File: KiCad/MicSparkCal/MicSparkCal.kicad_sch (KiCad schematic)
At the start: 36 parts, among them J1 Cortex Debug, J10 TF_S_A, J11 TF_S_B, J12 HV_A, J13 HV_B, J2 ON/OFF, J3 BOOST_IN_P, J4 BOOST_IN_N, J5 BOOST_OUT_P, J6 BOOST_OUT_N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

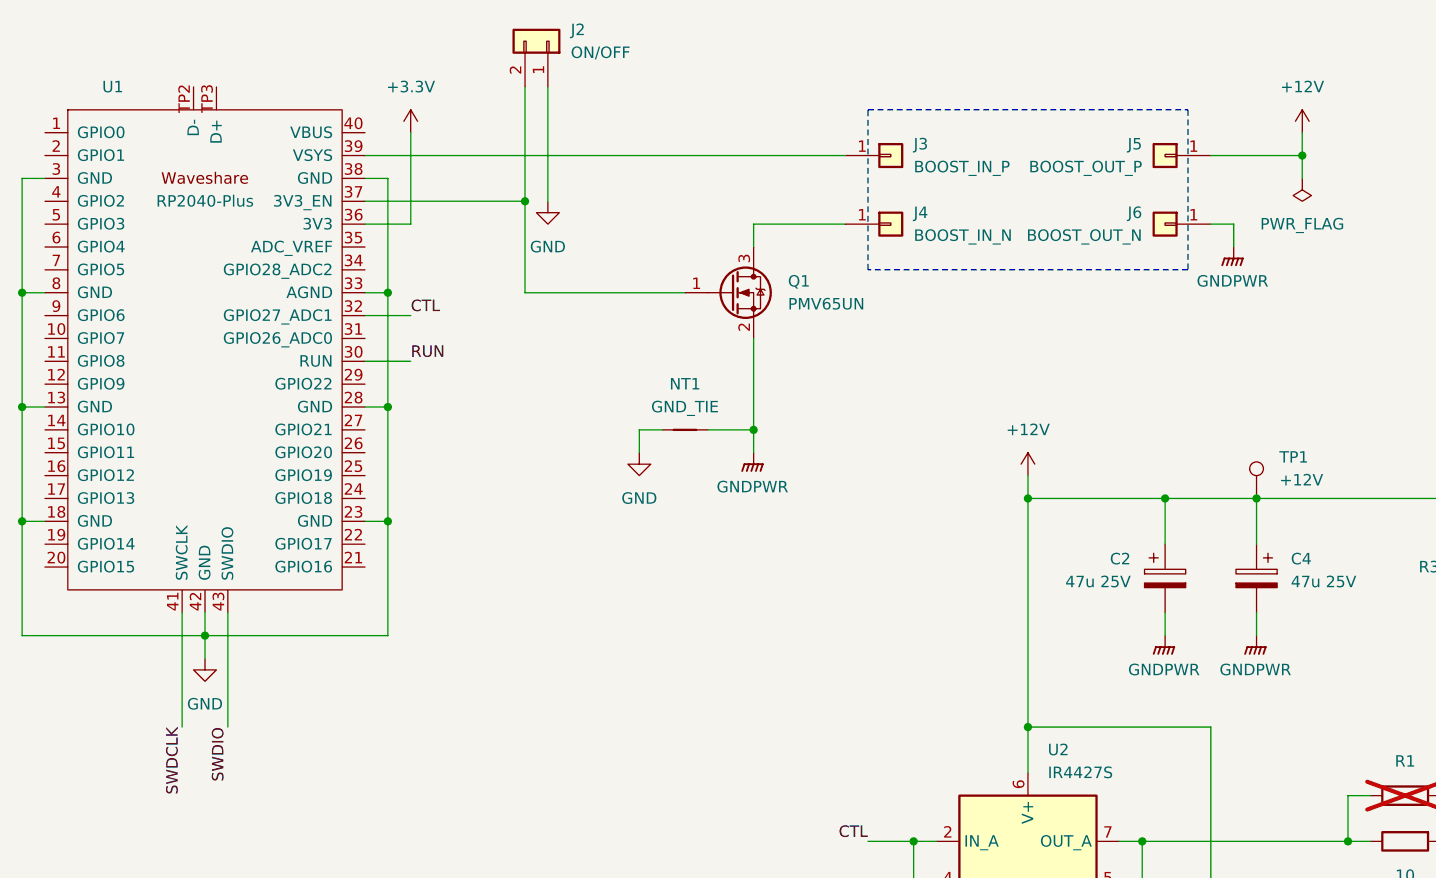
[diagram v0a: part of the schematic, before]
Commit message: Set h/w revision to 2 and include some fixes
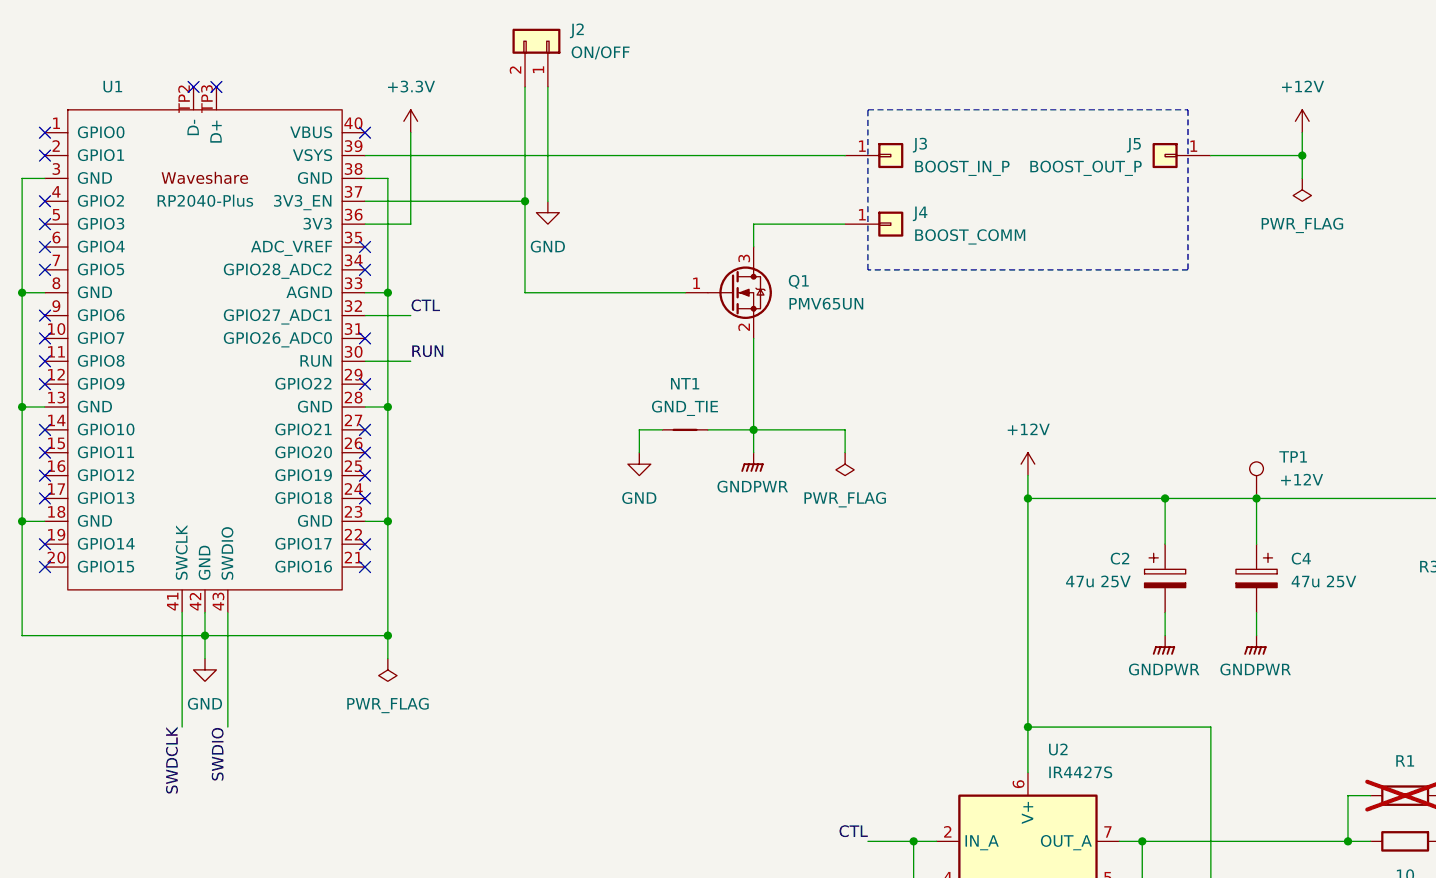
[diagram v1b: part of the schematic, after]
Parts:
- removed J6: BOOST_OUT_N, Connector_PinHeader_2.54mm:PinHeader_1x01_P2.54mm_Vertical, symbol Connector_Generic:Conn_01x01
- J4: value BOOST_IN_N -> BOOST_COMM
- U1: symbol RPi Pico:Waveshare_RP2040-Plus -> RP2040_boards:Waveshare_RP2040-Plus
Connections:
- no-connect marks 4 -> 33
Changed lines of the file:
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@@
 	(title_block
 		(title "Spark Generator")
-		(rev "1")
+		(rev "2")
 	)
 	(junction
@@
 	)
 	(junction
+		(at 71.12 91.44)
+		(diameter 0)
+		(color 0 0 0 0)
+	)
+	(junction
 		(at 266.7 95.25)
 		(diameter 0)
@@
 	)
 	(no_connect
+		(at 68.58 63.5)
+	)
+	(no_connect
+		(at 33.02 76.2)
+	)
+	(no_connect
+		(at 33.02 50.8)
+	)
+	(no_connect
+		(at 68.58 35.56)
+	)
+	(no_connect
+		(at 33.02 55.88)
+	)
+	(no_connect
+		(at 33.02 83.82)
+	)
+	(no_connect
+		(at 68.58 83.82)
+	)
+	(no_connect
+		(at 49.53 30.48)
+	)
+	(no_connect
+		(at 68.58 50.8)
+	)
+	(no_connect
+		(at 33.02 68.58)
+	)
+	(no_connect
 		(at 44.45 134.62)
 	)
 	(no_connect
+		(at 33.02 81.28)
+	)
+	(no_connect
+		(at 33.02 48.26)
+	)
+	(no_connect
+		(at 52.07 30.48)
+	)
+	(no_connect
+		(at 68.58 76.2)
+	)
+	(no_connect
+		(at 33.02 35.56)
+	)
+	(no_connect
+		(at 33.02 73.66)
+	)
+	(no_connect
+		(at 68.58 71.12)
+	)
+	(no_connect
+		(at 33.02 58.42)
+	)
+	(no_connect
+		(at 33.02 60.96)
+	)
+	(no_connect
+		(at 33.02 71.12)
+	)
+	(no_connect
+		(at 33.02 45.72)
+	)
+	(no_connect
+		(at 33.02 43.18)
+	)
+	(no_connect
+		(at 68.58 68.58)
+	)
+	(no_connect
+		(at 33.02 63.5)
+	)
+	(no_connect
+		(at 68.58 58.42)
+	)
+	(no_connect
+		(at 68.58 48.26)
+	)
+	(no_connect
 		(at 210.82 109.22)
 	)
@@
 		(at 57.15 134.62)
 	)
+	(no_connect
+		(at 68.58 73.66)
+	)
+	(no_connect
+		(at 68.58 81.28)
+	)
+	(no_connect
+		(at 33.02 38.1)
+	)
 	(wire
 		(pts
@@
 	(wire
 		(pts
-			(xy 165.1 45.72) (xy 162.56 45.72)
-		)
-		(stroke
-			(width 0)
-			(type default)
-		)
-	)
-	(wire
-		(pts
 			(xy 41.91 132.08) (xy 41.91 137.16)
 		)
@@
 	(wire
 		(pts
+			(xy 71.12 93.98) (xy 71.12 91.44)
+		)
+		(stroke
+			(width 0)
+			(type default)
+		)
+	)
+	(wire
+		(pts
 			(xy 41.91 127) (xy 41.91 124.46)
 		)
@@
 	(wire
 		(pts
+			(xy 121.92 71.12) (xy 121.92 68.58)
+		)
+		(stroke
+			(width 0)
+			(type default)
+		)
+	)
+	(wire
+		(pts
 			(xy 152.4 119.38) (xy 154.94 119.38)
 		)
@@
 	(wire
 		(pts
+			(xy 111.76 68.58) (xy 121.92 68.58)
+		)
+		(stroke
+			(width 0)
+			(type default)
+		)
+	)
+	(wire
+		(pts
 			(xy 68.58 40.64) (xy 71.12 40.64)
 		)
@@
 	(wire
 		(pts
-			(xy 165.1 48.26) (xy 165.1 45.72)
-		)
-		(stroke
-			(width 0)
-			(type default)
-		)
-	)
-	(wire
-		(pts
 			(xy 157.48 76.2) (xy 157.48 81.28)
 		)
@@
 	)
 	(symbol
-		(lib_id "power:GNDPWR")
-		(at 162.56 157.48 0)
+		(lib_id "power:PWR_FLAG")
+		(at 121.92 71.12 180)
 		(unit 1)
 		(exclude_from_sim no)
@@
 		(dnp no)
 		(fields_autoplaced yes)
-		(property "Reference" "#PWR011"
-			(at 162.56 162.56 0)
+		(property "Reference" "#FLG03"
+			(at 121.92 73.025 0)
 			(effects
 				(font
@@
 			)
 		)
-		(property "Value" "GNDPWR"
-			(at 162.433 161.29 0)
+		(property "Value" "PWR_FLAG"
+			(at 121.92 76.2 0)
 			(effects
 				(font
@@
 		)
 		(property "Footprint" ""
-			(at 162.56 158.75 0)
+			(at 121.92 71.12 0)
 			(effects
 				(font
@@
 			)
 		)
-		(property "Datasheet" ""
-			(at 162.56 158.75 0)
+		(property "Datasheet" "~"
+			(at 121.92 71.12 0)
 			(effects
 				(font
@@
 			)
 		)
-		(property "Description" "Power symbol creates a global label with name \"GNDPWR\" , global ground"
-			(at 162.56 157.48 0)
+		(property "Description" "Special symbol for telling ERC where power comes from"
+			(at 121.92 71.12 0)
 			(effects
 				(font
@@
 			(project "MicSparkCal"
 				(path "/0fcec650-ee01-49f6-8a2e-aeb2e1642de9"
-					(reference "#PWR011")
+					(reference "#FLG03")
 					(unit 1)
 				)
@@
 	)
 	(symbol
-		(lib_id "Connector_Generic:Conn_01x01")
-		(at 157.48 45.72 0)
-		(mirror y)
+		(lib_id "power:GNDPWR")
+		(at 162.56 157.48 0)
 		(unit 1)
 		(exclude_from_sim no)
@@
 		(on_board yes)
 		(dnp no)
-		(property "Reference" "J6"
-			(at 154.94 44.4499 0)
+		(fields_autoplaced yes)
+		(property "Reference" "#PWR011"
+			(at 162.56 162.56 0)
 			(effects
 				(font
 					(size 1.27 1.27)
 				)
-				(justify left)
+				(hide yes)
 			)
 		)
-		(property "Value" "BOOST_OUT_N"
-			(at 154.94 46.9899 0)
+		(property "Value" "GNDPWR"
+			(at 162.433 161.29 0)
 			(effects
 				(font
 					(size 1.27 1.27)
 				)
-				(justify left)
 			)
 		)
-		(property "Footprint" "Connector_PinHeader_2.54mm:PinHeader_1x01_P2.54mm_Vertical"
-			(at 157.48 45.72 0)
+		(property "Footprint" ""
+			(at 162.56 158.75 0)
 			(effects
 				(font
@@
 			)
 		)
-		(property "Datasheet" "~"
-			(at 157.48 45.72 0)
+		(property "Datasheet" ""
+			(at 162.56 158.75 0)
 			(effects
 				(font
@@
 			)
 		)
-		(property "Description" "Generic connector, single row, 01x01, script generated (kicad-library-utils/schlib/autogen/connector/)"
-			(at 157.48 45.72 0)
+		(property "Description" "Power symbol creates a global label with name \"GNDPWR\" , global ground"
+			(at 162.56 157.48 0)
 			(effects
 				(font
@@
 			(project "MicSparkCal"
 				(path "/0fcec650-ee01-49f6-8a2e-aeb2e1642de9"
-					(reference "J6")
+					(reference "#PWR011")
 					(unit 1)
 				)
@@
 	)
 	(symbol
-		(lib_id "power:GNDPWR")
-		(at 165.1 48.26 0)
-		(unit 1)
-		(exclude_from_sim no)
-		(in_bom yes)
-		(on_board yes)
-		(dnp no)
-		(fields_autoplaced yes)
-		(property "Reference" "#PWR012"
-			(at 165.1 53.34 0)
-			(effects
-				(font
-					(size 1.27 1.27)
-				)
-				(hide yes)
-			)
-		)
-		(property "Value" "GNDPWR"
-			(at 164.973 52.07 0)
-			(effects
-				(font
-					(size 1.27 1.27)
-				)
-			)
-		)
-		(property "Footprint" ""
-			(at 165.1 49.53 0)
-			(effects
-				(font
-					(size 1.27 1.27)
-				)
-				(hide yes)
-			)
-		)
-		(property "Datasheet" ""
-			(at 165.1 49.53 0)
-			(effects
-				(font
-					(size 1.27 1.27)
-				)
-				(hide yes)
-			)
-		)
-		(property "Description" "Power symbol creates a global label with name \"GNDPWR\" , global ground"
-			(at 165.1 48.26 0)
-			(effects
-				(font
-					(size 1.27 1.27)
-				)
-				(hide yes)
-			)
-		)
-		(pin "1"
-		)
-		(instances
-			(project "MicSparkCal"
-				(path "/0fcec650-ee01-49f6-8a2e-aeb2e1642de9"
-					(reference "#PWR012")
-					(unit 1)
-				)
-			)
-		)
-	)
-	(symbol
 		(lib_id "Device:C")
 		(at 257.81 120.65 90)
@@
 	)
 	(symbol
+		(lib_id "power:PWR_FLAG")
+		(at 71.12 93.98 180)
+		(unit 1)
+		(exclude_from_sim no)
+		(in_bom yes)
+		(on_board yes)
+		(dnp no)
+		(fields_autoplaced yes)
+		(property "Reference" "#FLG02"
+			(at 71.12 95.885 0)
+			(effects
+				(font
+					(size 1.27 1.27)
+				)
+				(hide yes)
+			)
+		)
+		(property "Value" "PWR_FLAG"
+			(at 71.12 99.06 0)
+			(effects
+				(font
+					(size 1.27 1.27)
+				)
+			)
+		)
+		(property "Footprint" ""
+			(at 71.12 93.98 0)
+			(effects
+				(font
+					(size 1.27 1.27)
+				)
+				(hide yes)
+			)
+		)
+		(property "Datasheet" "~"
+			(at 71.12 93.98 0)
+			(effects
+				(font
+					(size 1.27 1.27)
+				)
+				(hide yes)
+			)
+		)
+		(property "Description" "Special symbol for telling ERC where power comes from"
+			(at 71.12 93.98 0)
+			(effects
+				(font
+					(size 1.27 1.27)
+				)
+				(hide yes)
+			)
+		)
+		(pin "1"
+		)
+		(instances
+			(project "MicSparkCal"
+				(path "/0fcec650-ee01-49f6-8a2e-aeb2e1642de9"
+					(reference "#FLG02")
+					(unit 1)
+				)
+			)
+		)
+	)
+	(symbol
 		(lib_id "power:GND")
 		(at 99.06 71.12 0)
@@
 			)
 		)
-		(property "Value" "BOOST_IN_N"
+		(property "Value" "BOOST_COMM"
 			(at 129.54 46.9899 0)
 			(effects
@@
 	)
 	(symbol
-		(lib_id "RPi Pico:Waveshare_RP2040-Plus")
+		(lib_id "RP2040_boards:Waveshare_RP2040-Plus")
 		(at 50.8 59.69 0)
 		(unit 1)
